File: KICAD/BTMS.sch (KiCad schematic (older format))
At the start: 315 parts, among them J1 fan, J10 U1COMMS, J11 U2COMMS, J13 IntBTemp, J14 ctrlTemp, J15 12Vout, J16 12Vin, J17 5Vout, J2 mContactor, J3 Tac, J5 ICSP, J7 5Vout, J9 key, Q1 PSMN5R6-100BS, Q10 PSMN5R6-100BS, Q11 DMN65D8L, Q12 DMN65D8L, Q13 FDN340P, Q14 ZXTP2025FTA, Q15 ZXTP2025FTA, Q16 ZXTP2025FTA, Q17 DMN65D8L, Q18 DMN65D8L, Q2 PSMN5R6-100BS, Q3 PSMN5R6-100BS, Q4 DMN65D8L, Q5 DMN65D8L, Q6 DMN65D8L, Q7 DMN65D8L, Q8 PSMN5R6-100BS, Q9 FDN340P, U1 R-78HB12-0.5, U10 A41AS12VDC, U11 A41AS12VDC, U12 A41AS12VDC, U13 A41AS12VDC, U14 A41AS12VDC, U15 NL17SZ74USG, U2 ACS780xLRTR-050B, U3 UCC27201DDAR, U4 FAN3111ESX, U5 HCPL-3120, U6 L7805CV, U7 LTV-817S, U8 dsPIC30F3011-PT, U9 LM62CIM3/NOPB

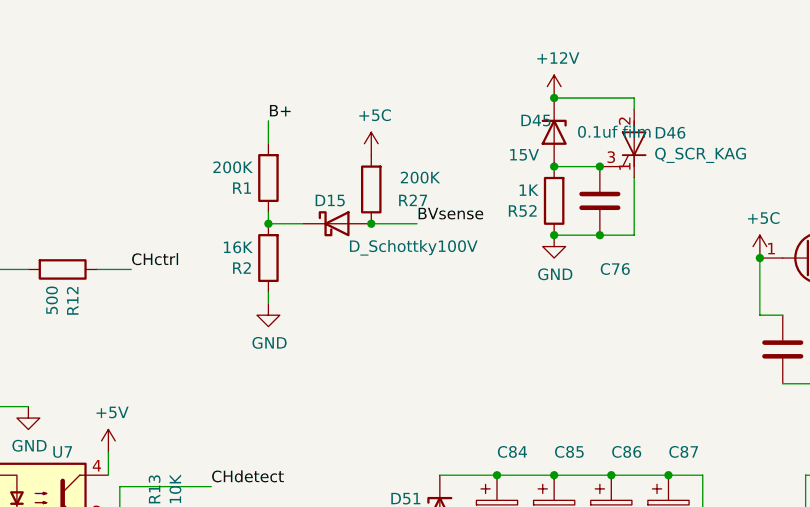
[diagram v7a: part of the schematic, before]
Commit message: Updated battery voltage divider.
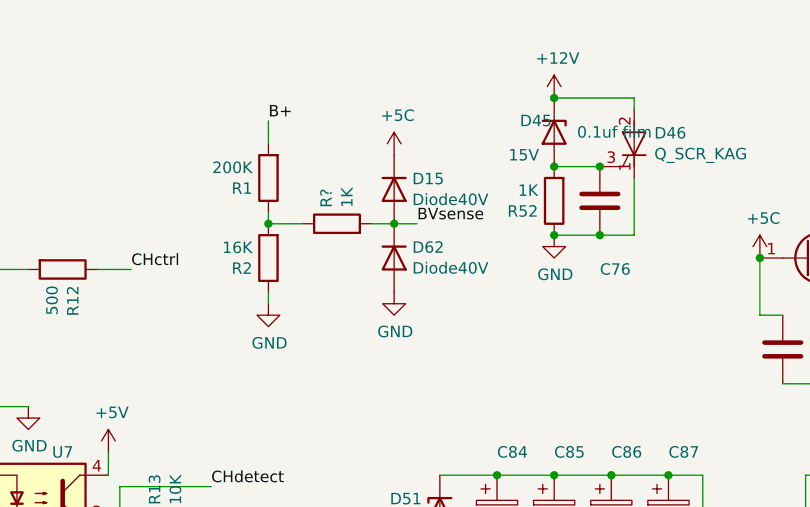
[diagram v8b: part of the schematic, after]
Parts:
- removed D15: D_Schottky100V, Diodes_SMD:D_SOD-123, symbol Device:D_Schottky
- removed R27: 200K, Resistors_SMD:R_0603, symbol Device:R
- added D15, D62: Diode40V, Diodes_SMD:D_0603, symbol Device:D
- added R?: 1K, Resistors_SMD:R_0603, symbol Device:R
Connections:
- net +5C: now also D15.1 (K)
- net BVsense: now also D15.2 (A), D62.1 (K), R?.2
- net GND: now also D62.2 (A)
- net at R1.1, R2.2: now also R?.1
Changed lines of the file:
@@
 Connection ~ 5350 1300
-$Comp
-L Device:R R27
-U 1 1 6036EF53
-P 5800 1150
-F 0 "R27" H 5550 1200 50  0000 L CNN
-F 1 "200K" H 5500 1100 50  0000 L CNN
-F 2 "Resistors_SMD:R_0603" V 5730 1150 50  0001 C CNN
-F 3 "~" H 5800 1150 50  0001 C CNN
-F 4 "https://www.digikey.com/en/products/detail/panasonic-electronic-components/ERJ-PA3F2003V/5035886" H 5800 1150 50  0001 C CNN "DK_Detail_Page"
-F 5 "P200KBYCT-ND" H 5800 1150 50  0001 C CNN "Digi-Key_PN"
-	1    5800 1150
-	-1   0    0    1
-$EndComp
 $Comp
 L power:+5C #PWR0116
 U 1 1 6036F5E3
-P 5800 1000
-F 0 "#PWR0116" H 5800 850 50  0001 C CNN
-F 1 "+5C" H 5815 1173 50  0000 C CNN
-F 2 "" H 5800 1000 50  0001 C CNN
-F 3 "" H 5800 1000 50  0001 C CNN
-	1    5800 1000
-	1    0    0    -1
-$EndComp
-Wire Wire Line
-	6000 1300 5800 1300
+P 5900 1000
+F 0 "#PWR0116" H 5900 850 50  0001 C CNN
+F 1 "+5C" H 5915 1173 50  0000 C CNN
+F 2 "" H 5900 1000 50  0001 C CNN
+F 3 "" H 5900 1000 50  0001 C CNN
+	1    5900 1000
+	1    0    0    -1
+$EndComp
 $Comp
 L Device:CP C84
@@
 Connection ~ 11800 1700
 $Comp
-L Device:D_Schottky D15
-U 1 1 60390ABA
-P 5650 1300
-F 0 "D15" H 5550 1400 50  0000 L CNN
-F 1 "D_Schottky100V" H 5700 1200 50  0000 L CNN
-F 2 "Diodes_SMD:D_SOD-123" H 5650 1300 50  0001 C CNN
-F 3 "~" H 5650 1300 50  0001 C CNN
-F 4 "https://www.digikey.com/en/products/detail/micro-commercial-co/MBR0580-TP/2423323" H 5650 1300 50  0001 C CNN "DK_Detail_Page"
-F 5 "MBR0580-TPMSCT-ND" H 5650 1300 50  0001 C CNN "Digi-Key_PN"
-	1    5650 1300
-	1    0    0    -1
-$EndComp
-Connection ~ 5800 1300
-$Comp
 L Device:D_Schottky D57
 U 1 1 603AE2E8
@@
 	0    -1   -1   0
 $EndComp
+$Comp
+L power:GND #PWR07
+U 1 1 621298A5
+P 5900 1600
+F 0 "#PWR07" H 5900 1350 50  0001 C CNN
+F 1 "GND" H 5905 1427 50  0000 C CNN
+F 2 "" H 5900 1600 50  0001 C CNN
+F 3 "" H 5900 1600 50  0001 C CNN
+	1    5900 1600
+	1    0    0    -1
+$EndComp
+$Comp
+L Device:D D15
+U 1 1 6212D514
+P 5900 1150
+F 0 "D15" V 5854 1229 50  0000 L CNN
+F 1 "Diode40V" V 5945 1229 50  0000 L CNN
+F 2 "Diodes_SMD:D_0603" H 5900 1150 50  0001 C CNN
+F 3 "~" H 5900 1150 50  0001 C CNN
+F 4 "https://www.digikey.com/en/products/detail/toshiba-semiconductor-and-storage/CCS15S40L3F/5210646" H 5900 1150 50  0001 C CNN "DK_Detail_Page"
+F 5 "CCS15S40L3FCT-ND" H 5900 1150 50  0001 C CNN "Digi-Key_PN"
+	1    5900 1150
+	0    1    1    0
+$EndComp
+Wire Wire Line
+	5800 1300 5900 1300
+Connection ~ 5900 1300
+Wire Wire Line
+	5900 1300 6000 1300
+$Comp
+L Device:D D62
+U 1 1 6212F823
+P 5900 1450
+F 0 "D62" V 5854 1529 50  0000 L CNN
+F 1 "Diode40V" V 5945 1529 50  0000 L CNN
+F 2 "Diodes_SMD:D_0603" H 5900 1450 50  0001 C CNN
+F 3 "~" H 5900 1450 50  0001 C CNN
+F 4 "https://www.digikey.com/en/products/detail/toshiba-semiconductor-and-storage/CCS15S40L3F/5210646" H 5900 1450 50  0001 C CNN "DK_Detail_Page"
+F 5 "CCS15S40L3FCT-ND" H 5900 1450 50  0001 C CNN "Digi-Key_PN"
+	1    5900 1450
+	0    1    1    0
+$EndComp
+$Comp
+L Device:R R?
+U 1 1 62134C51
+P 5650 1300
+F 0 "R?" H 5720 1346 50  0000 L CNN
+F 1 "1K" H 5720 1255 50  0000 L CNN
+F 2 "Resistors_SMD:R_0603" V 5580 1300 50  0001 C CNN
+F 3 "~" H 5650 1300 50  0001 C CNN
+F 4 "https://www.digikey.com/en/products/detail/te-connectivity-passive-product/CRGP0603F1K0/8577018" H 5650 1300 50  0001 C CNN "DK_Detail_Page"
+F 5 "A130416CT-ND" H 5650 1300 50  0001 C CNN "Digi-Key_PN"
+	1    5650 1300
+	0    -1   -1   0
+$EndComp
